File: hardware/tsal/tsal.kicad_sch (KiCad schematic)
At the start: 66 parts, among them J1 Conn_01x02, J2 Conn_01x02, J3 Conn_01x02, J4 Conn_01x02, J5 Conn_01x03, J6 Conn_01x04, J7 Conn_01x02, Q1 BUK7M9R5-40H, Q2 BUK7M9R5-40H, U1 4081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

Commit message: Made some progress on the PCB
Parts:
- J1, J2, J3, J4, J7: footprint Connector_PinSocket_2.54mm:PinSocket_1x02_P2.54mm_Horizontal -> Connector_Molex:Molex_Micro-Fit_3.0_43650-0200_1x02_P3.00mm_Horizontal
- J5: footprint Connector_PinSocket_2.54mm:PinSocket_1x03_P2.54mm_Horizontal -> Connector_Molex:Molex_Micro-Fit_3.0_43650-0300_1x03_P3.00mm_Horizontal
- J6: footprint Connector_PinSocket_2.54mm:PinSocket_1x04_P2.54mm_Horizontal -> Connector_Molex:Molex_Micro-Fit_3.0_43650-0400_1x04_P3.00mm_Horizontal
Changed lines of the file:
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@@
     (property "Reference" "J1" (id 0) (at 32.385 20.32 0))
     (property "Value" "Conn_01x02" (id 1) (at 32.385 22.86 0))
-    (property "Footprint" "Connector_PinSocket_2.54mm:PinSocket_1x02_P2.54mm_Horizontal" (id 2) (at 32.385 29.21 0)
+    (property "Footprint" "Connector_Molex:Molex_Micro-Fit_3.0_43650-0200_1x02_P3.00mm_Horizontal" (id 2) (at 32.385 29.21 0)
       (effects (font (size 1.27 1.27)) hide)
     )
@@
     (property "Reference" "J5" (id 0) (at 153.67 71.755 0))
     (property "Value" "Conn_01x03" (id 1) (at 153.67 74.295 0))
-    (property "Footprint" "Connector_PinSocket_2.54mm:PinSocket_1x03_P2.54mm_Horizontal" (id 2) (at 153.67 80.645 0)
+    (property "Footprint" "Connector_Molex:Molex_Micro-Fit_3.0_43650-0300_1x03_P3.00mm_Horizontal" (id 2) (at 153.67 80.645 0)
       (effects (font (size 1.27 1.27)) hide)
     )
@@
     (property "Reference" "J3" (id 0) (at 75.565 84.455 0))
     (property "Value" "Conn_01x02" (id 1) (at 74.803 86.741 0))
-    (property "Footprint" "Connector_PinSocket_2.54mm:PinSocket_1x02_P2.54mm_Horizontal" (id 2) (at 75.565 81.915 0)
+    (property "Footprint" "Connector_Molex:Molex_Micro-Fit_3.0_43650-0200_1x02_P3.00mm_Horizontal" (id 2) (at 75.565 81.915 0)
       (effects (font (size 1.27 1.27)) hide)
     )
@@
     (property "Reference" "J7" (id 0) (at 363.22 189.865 0))
     (property "Value" "Conn_01x02" (id 1) (at 364.49 186.69 0))
-    (property "Footprint" "Connector_PinSocket_2.54mm:PinSocket_1x02_P2.54mm_Horizontal" (id 2) (at 355.6 186.055 0)
+    (property "Footprint" "Connector_Molex:Molex_Micro-Fit_3.0_43650-0200_1x02_P3.00mm_Horizontal" (id 2) (at 355.6 186.055 0)
       (effects (font (size 1.27 1.27)) hide)
     )
@@
     (property "Reference" "J2" (id 0) (at 27.94 78.74 0))
     (property "Value" "Conn_01x02" (id 1) (at 26.67 81.915 0))
-    (property "Footprint" "Connector_PinSocket_2.54mm:PinSocket_1x02_P2.54mm_Horizontal" (id 2) (at 35.56 82.55 0)
+    (property "Footprint" "Connector_Molex:Molex_Micro-Fit_3.0_43650-0200_1x02_P3.00mm_Horizontal" (id 2) (at 35.56 82.55 0)
       (effects (font (size 1.27 1.27)) hide)
     )
@@
     (property "Reference" "J4" (id 0) (at 111.76 85.09 0))
     (property "Value" "Conn_01x02" (id 1) (at 111.125 86.995 0))
-    (property "Footprint" "Connector_PinSocket_2.54mm:PinSocket_1x02_P2.54mm_Horizontal" (id 2) (at 112.395 81.915 0)
+    (property "Footprint" "Connector_Molex:Molex_Micro-Fit_3.0_43650-0200_1x02_P3.00mm_Horizontal" (id 2) (at 112.395 81.915 0)
       (effects (font (size 1.27 1.27)) hide)
     )
@@
       (effects (font (size 1.27 1.27)) (justify left))
     )
-    (property "Footprint" "Connector_PinSocket_2.54mm:PinSocket_1x04_P2.54mm_Horizontal" (id 2) (at 248.285 66.675 0)
+    (property "Footprint" "Connector_Molex:Molex_Micro-Fit_3.0_43650-0400_1x04_P3.00mm_Horizontal" (id 2) (at 248.285 66.675 0)
       (effects (font (size 1.27 1.27)) hide)
     )
@@
     )
     (path "/286203f6-cf6b-4d22-b903-be37d0b23cb3"
-      (reference "J1") (unit 1) (value "Conn_01x02") (footprint "Connector_PinSocket_2.54mm:PinSocket_1x02_P2.54mm_Horizontal")
+      (reference "J1") (unit 1) (value "Conn_01x02") (footprint "Connector_Molex:Molex_Micro-Fit_3.0_43650-0200_1x02_P3.00mm_Horizontal")
     )
     (path "/5571bd08-df8d-4394-9b10-eadfc0d72d48"
-      (reference "J2") (unit 1) (value "Conn_01x02") (footprint "Connector_PinSocket_2.54mm:PinSocket_1x02_P2.54mm_Horizontal")
+      (reference "J2") (unit 1) (value "Conn_01x02") (footprint "Connector_Molex:Molex_Micro-Fit_3.0_43650-0200_1x02_P3.00mm_Horizontal")
     )
     (path "/4474fed7-976b-40f4-b120-9118e7903a61"
-      (reference "J3") (unit 1) (value "Conn_01x02") (footprint "Connector_PinSocket_2.54mm:PinSocket_1x02_P2.54mm_Horizontal")
+      (reference "J3") (unit 1) (value "Conn_01x02") (footprint "Connector_Molex:Molex_Micro-Fit_3.0_43650-0200_1x02_P3.00mm_Horizontal")
     )
     (path "/a40a808c-e9ae-4b26-9fcc-2e500db65767"
-      (reference "J4") (unit 1) (value "Conn_01x02") (footprint "Connector_PinSocket_2.54mm:PinSocket_1x02_P2.54mm_Horizontal")
+      (reference "J4") (unit 1) (value "Conn_01x02") (footprint "Connector_Molex:Molex_Micro-Fit_3.0_43650-0200_1x02_P3.00mm_Horizontal")
     )
     (path "/3a4bbc77-f599-40c3-b08a-510d903ef6a7"
-      (reference "J5") (unit 1) (value "Conn_01x03") (footprint "Connector_PinSocket_2.54mm:PinSocket_1x03_P2.54mm_Horizontal")
+      (reference "J5") (unit 1) (value "Conn_01x03") (footprint "Connector_Molex:Molex_Micro-Fit_3.0_43650-0300_1x03_P3.00mm_Horizontal")
     )
     (path "/bd516739-a80b-4d06-89c5-c02060698459"
-      (reference "J6") (unit 1) (value "Conn_01x04") (footprint "Connector_PinSocket_2.54mm:PinSocket_1x04_P2.54mm_Horizontal")
+      (reference "J6") (unit 1) (value "Conn_01x04") (footprint "Connector_Molex:Molex_Micro-Fit_3.0_43650-0400_1x04_P3.00mm_Horizontal")
     )
     (path "/4daaa113-639b-4fd0-9c35-a1da002f58a7"
-      (reference "J7") (unit 1) (value "Conn_01x02") (footprint "Connector_PinSocket_2.54mm:PinSocket_1x02_P2.54mm_Horizontal")
+      (reference "J7") (unit 1) (value "Conn_01x02") (footprint "Connector_Molex:Molex_Micro-Fit_3.0_43650-0200_1x02_P3.00mm_Horizontal")
     )
     (path "/d807ab4e-782e-412a-a12e-09a77b8c3305"

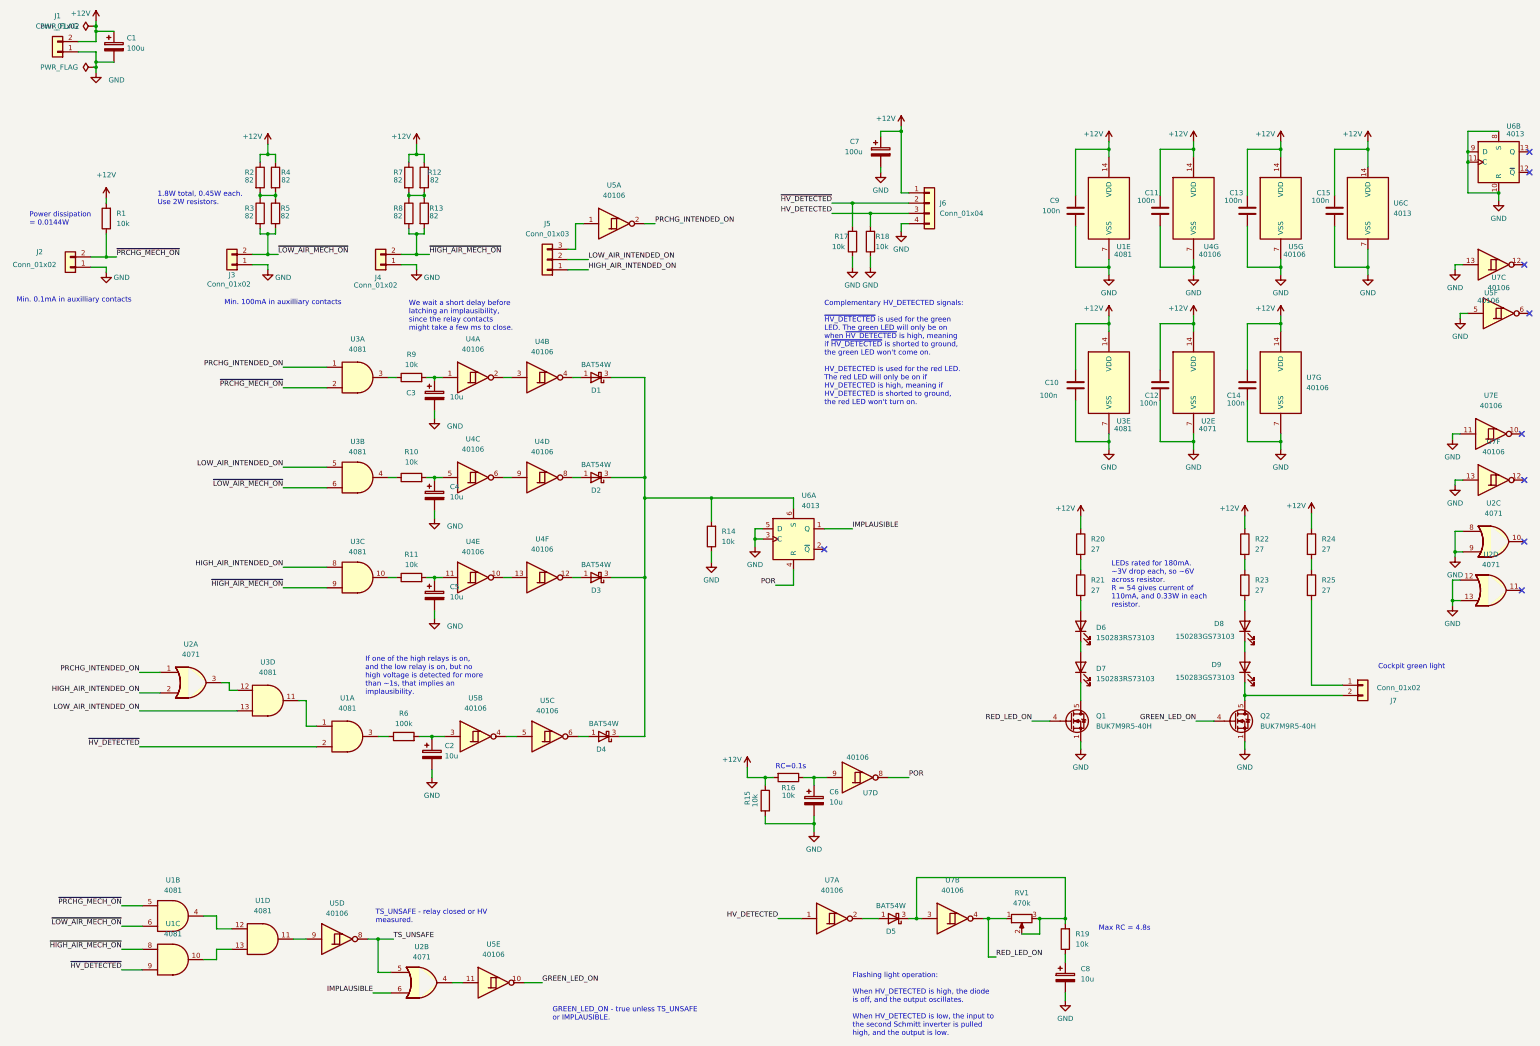
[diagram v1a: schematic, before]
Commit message: Designed and finished layout of TSAL
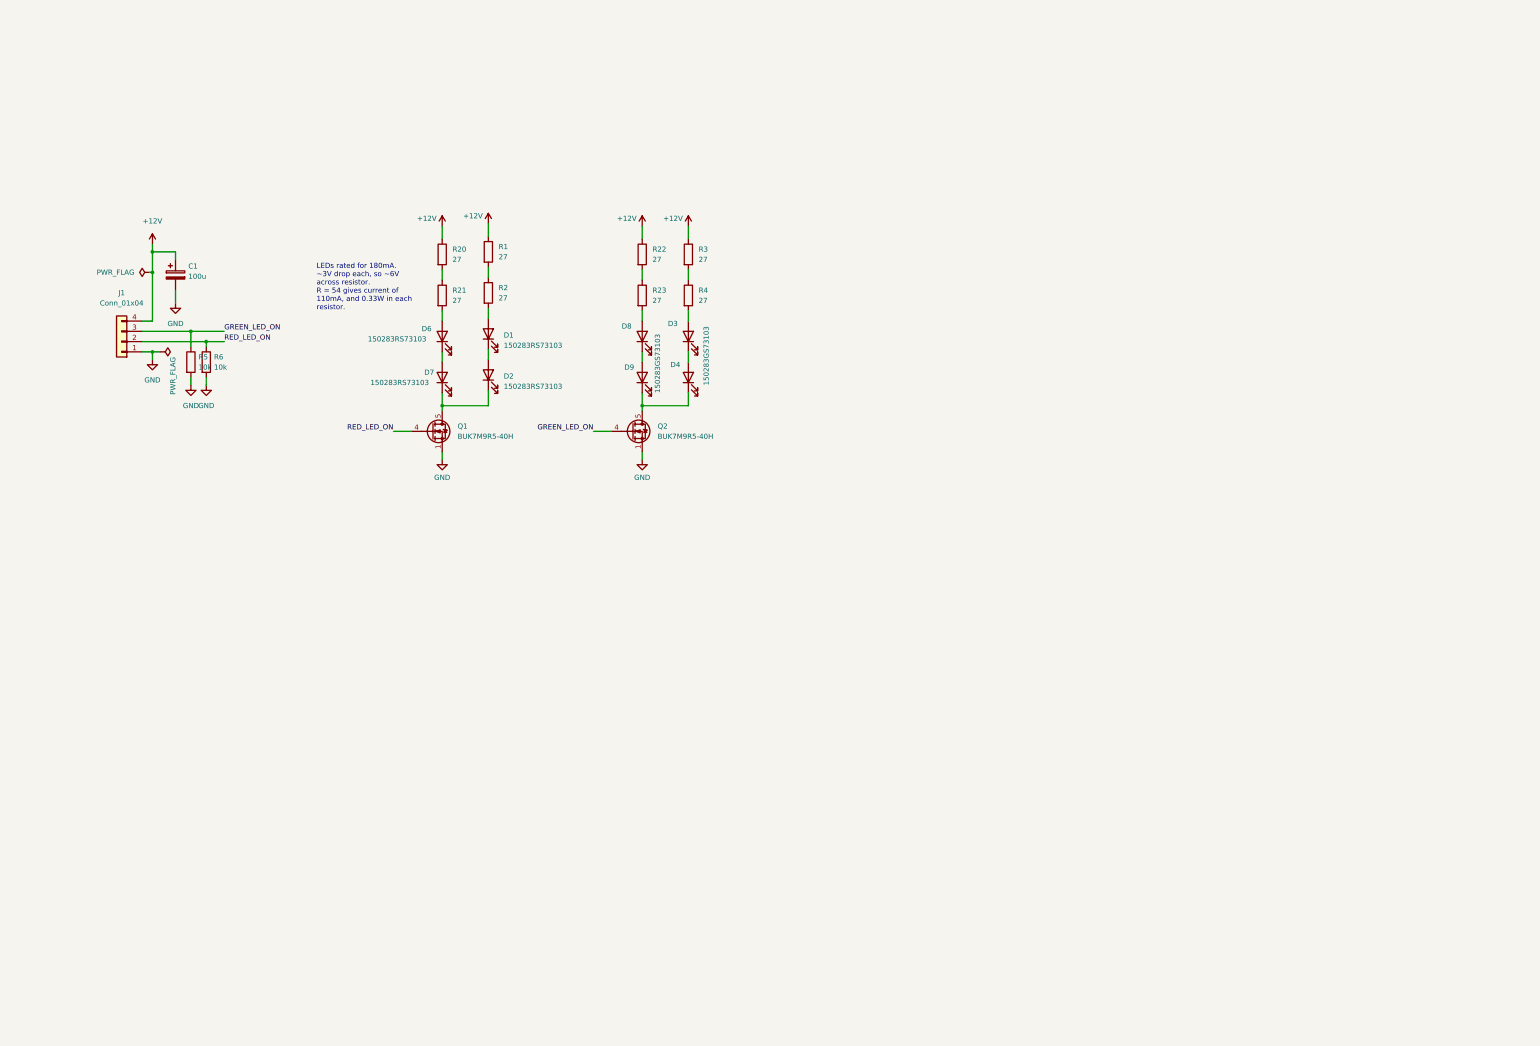
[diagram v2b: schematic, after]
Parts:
- removed C10, C11, C12, C13, C14, C15, C9: 100n, Capacitor_SMD:C_0603_1608Metric, symbol Device:C
- removed C2, C3, C4, C5, C6, C8: 10u, Capacitor_THT:CP_Radial_D5.0mm_P2.00mm, symbol Device:C_Polarized
- removed C7: 100u, Capacitor_THT:CP_Radial_D6.3mm_P2.50mm, symbol Device:C_Polarized
- removed D1, D2, D3, D4, D5: BAT54W, Package_TO_SOT_SMD:SOT-323_SC-70, symbol Diode:BAT54W
- removed J1, J2, J3, J4, J7: Conn_01x02, Connector_Molex:Molex_Micro-Fit_3.0_43650-0200_1x02_P3.00mm_Horizontal, symbol Connector_Generic:Conn_01x02
- removed J5: Conn_01x03, Connector_Molex:Molex_Micro-Fit_3.0_43650-0300_1x03_P3.00mm_Horizontal, symbol Connector_Generic:Conn_01x03
- removed J6: Conn_01x04, Connector_Molex:Molex_Micro-Fit_3.0_43650-0400_1x04_P3.00mm_Horizontal, symbol Connector_Generic:Conn_01x04
- removed R10, R11, R14, R15, R16, R17, R18, R19, R9: 10k, Resistor_SMD:R_0603_1608Metric, symbol Device:R
- removed R12, R13, R7, R8: 82, Resistor_SMD:R_2512_6332Metric, symbol Device:R
- removed R24, R25: 27, Resistor_SMD:R_2512_6332Metric, symbol Device:R
- removed RV1: 470k, Potentiometer_THT:Potentiometer_Bourns_3296W_Vertical, symbol Device:R_Potentiometer
- removed U1, U3: 4081, Package_SO:SOIC-14_3.9x8.7mm_P1.27mm, symbol 4xxx:4081
- removed U2: 4071, Package_SO:SOIC-14_3.9x8.7mm_P1.27mm, symbol 4xxx:4071
- removed U4, U5, U7: 40106, Package_SO:SOIC-14_3.9x8.7mm_P1.27mm, symbol 4xxx:40106
- removed U6: 4013, Package_SO:SOIC-14_3.9x8.7mm_P1.27mm, symbol 4xxx:4013
- added D1, D2: 150283RS73103, footprints:Wurth_WL-SMTW, symbol Device:LED
- added D3, D4: 150283GS73103, footprints:Wurth_WL-SMTW, symbol Device:LED
- added J1: Conn_01x04, Connector_Molex:Molex_Micro-Fit_3.0_43650-0400_1x04_P3.00mm_Horizontal, symbol Connector_Generic:Conn_01x04
- R1: value 10k -> 27; footprint Resistor_SMD:R_0603_1608Metric -> Resistor_SMD:R_2512_6332Metric
- R2, R3, R4: value 82 -> 27
- R5: value 82 -> 10k; footprint Resistor_SMD:R_2512_6332Metric -> Resistor_SMD:R_0603_1608Metric
- R6: value 100k -> 10k
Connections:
- net ~{PRCHG_MECH_ON} is gone; now on net +12V: R1.1
- net +12V: now also R3.1, J1.4 (Pin_4); no longer R1.2, R2.1, R4.1
- net GND: now also R5.2, R6.2, J1.1 (Pin_1)
- net GREEN_LED_ON: now also R5.1, J1.3 (Pin_3)
- net RED_LED_ON: now also R6.1, J1.2 (Pin_2)
- net at D9.1 (K), Q2.5 (D): now also D4.1 (K)
- net at D7.1 (K), Q1.5 (D): now also D2.1 (K)
- net ~{LOW_AIR_MECH_ON}: no longer names the net of R3.2
- net ~{LOW_AIR_MECH_ON}: now also R4.1; no longer R5.2
- new net: D3.2 (A), R4.2
- new net: R1.2, R2.1
- new net: D1.2 (A), R2.2
- new net: D3.1 (K), D4.2 (A)
- new net: D1.1 (K), D2.2 (A)
- no-connect marks 9 -> 0
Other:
- note removed: "1.8W total, 0.45W each. Use 2W resistors."
- note removed: "Cockpit green light"
- note removed: "Complementary HV_DETECTED signals: ~{HV_DETECTED} is used for the green LED. The green LED will only be on when ~{HV_DETECTED} is high, meaning if ~{HV_DETECTED} is shorted to ground, the green LED won't come on. HV_DETECTED is used for the red LED. The red LED will only be on if HV_DETECTED is high, meaning if HV_DETECTED is shorted to ground, the red LED won't turn on."
- note removed: "Flashing light operation: When HV_DETECTED is high, the diode is off, and the output oscillates. When HV_DETECTED is low, the input to the second Schmitt inverter is pulled high, and the output is low."
- note removed: "GREEN_LED_ON - true unless TS_UNSAFE or IMPLAUSIBLE."
- note removed: "If one of the high relays is on, and the low relay is on, but no high voltage is detected for more than ~1s, that implies an implausibility."
- note removed: "Max RC = 4.8s"
- note removed: "Min. 0.1mA in auxilliary contacts"
- note removed: "Min. 100mA in auxilliary contacts"
- note removed: "Power dissipation = 0.0144W"
- note removed: "RC=0.1s"
- note removed: "TS_UNSAFE - relay closed or HV measured."
- note removed: "We wait a short delay before latching an implausibility, since the relay contacts might take a few ms to close."
- moved on the sheet: D6, D7, D8, D9, Q1, Q2, R20, R21, R22, R23
